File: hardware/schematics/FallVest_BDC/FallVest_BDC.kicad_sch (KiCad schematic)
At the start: 5 parts, among them U1 STP55NF06L, U3 4554

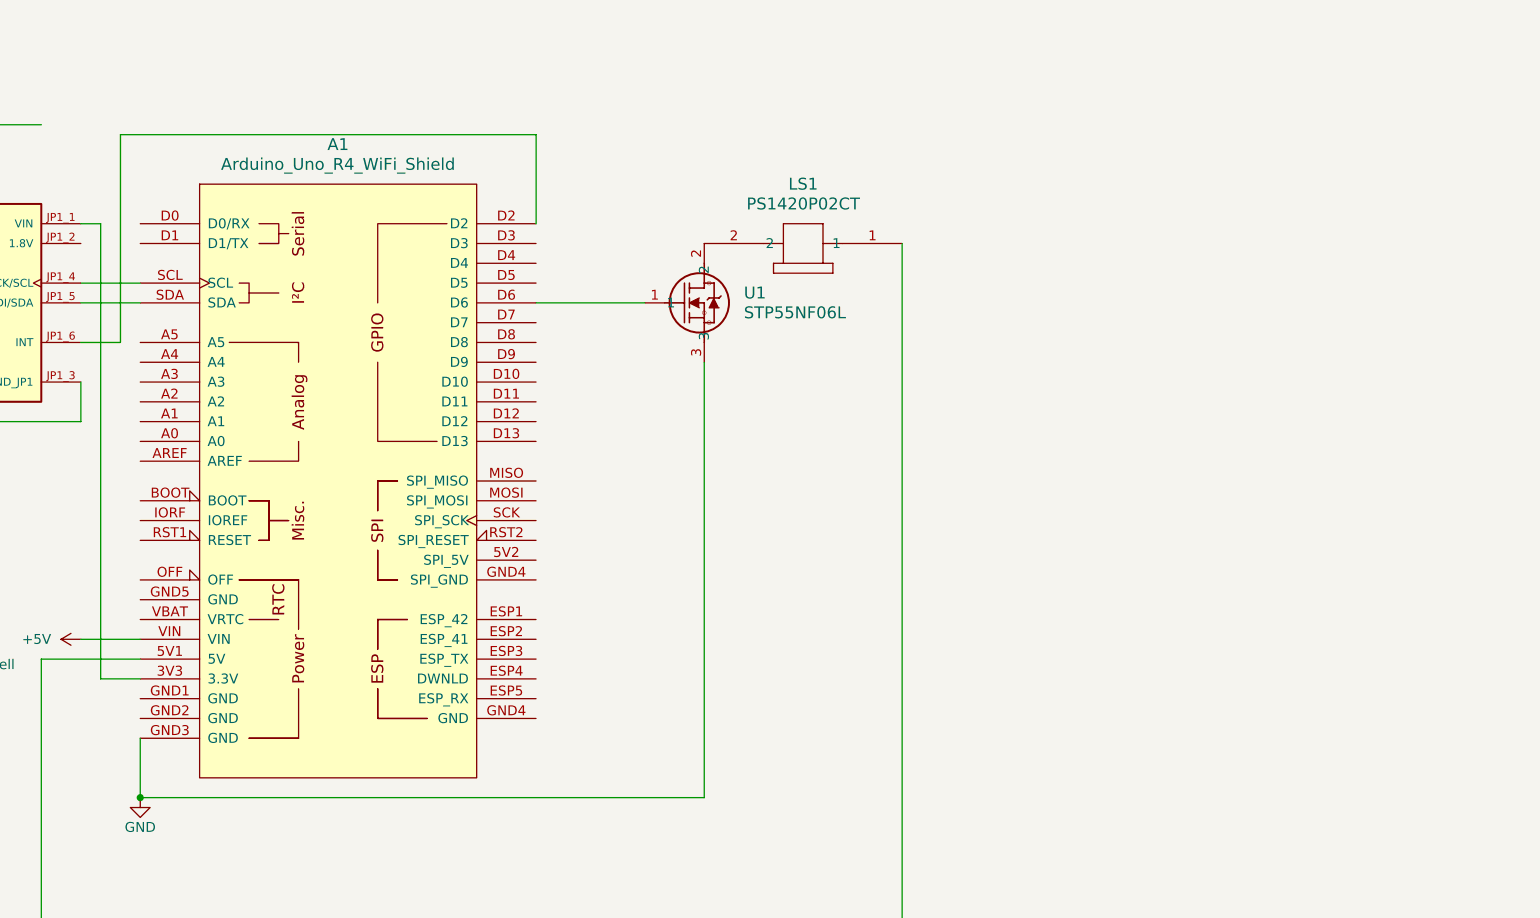
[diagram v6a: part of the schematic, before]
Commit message: Hardware Change
Replaced Uno with ESP 32
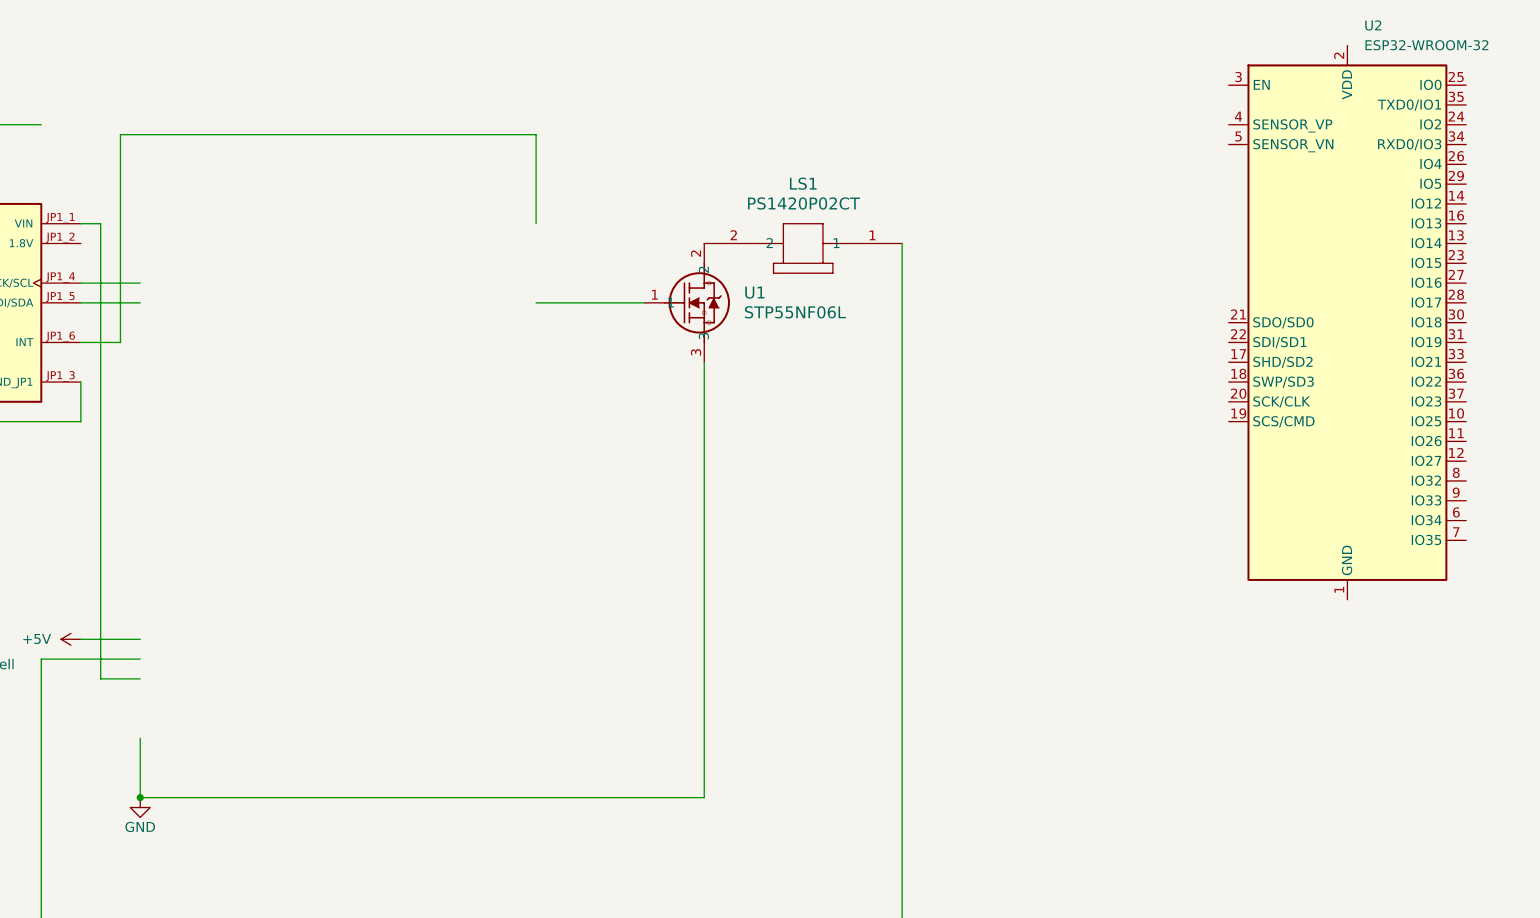
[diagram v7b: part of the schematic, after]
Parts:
- removed A1: Arduino_Uno_R4_WiFi_Shield, PCM_arduino-library:Arduino_Uno_R4_WiFi_Shield, symbol arduino-library:Arduino_Uno_R4_WiFi_Shield
- added U2: ESP32-WROOM-32, RF_Module:ESP32-WROOM-32, symbol RF_Module:ESP32-WROOM-32
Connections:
- new net: U2.1 (GND), U2.15 (GND), U2.38 (GND), U2.39 (GND)
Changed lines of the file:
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@@
+	)
+	(symbol
+		(lib_id "RF_Module:ESP32-WROOM-32")
+		(at 256.54 60.96 0)
+		(unit 1)
+		(exclude_from_sim no)
+		(in_bom yes)
+		(on_board yes)
+		(dnp no)
+		(fields_autoplaced yes)
+		(property "Reference" "U2"
+			(at 258.6833 22.86 0)
+			(effects
+				(font
+					(size 1.27 1.27)
+				)
+				(justify left)
+			)
+		)
+		(property "Value" "ESP32-WROOM-32"
+			(at 258.6833 25.4 0)
+			(effects
+				(font
+					(size 1.27 1.27)
+				)
+				(justify left)
+			)
+		)
+		(property "Footprint" "RF_Module:ESP32-WROOM-32"
+			(at 256.54 99.06 0)
+			(effects
+				(font
+					(size 1.27 1.27)
+				)
+				(hide yes)
+			)
+		)
+		(property "Datasheet" "https://www.espressif.com/sites/default/files/documentation/esp32-wroom-32_datasheet_en.pdf"
+			(at 248.92 59.69 0)
+			(effects
+				(font
+					(size 1.27 1.27)
+				)
+				(hide yes)
+			)
+		)
+		(property "Description" "RF Module, ESP32-D0WDQ6 SoC, Wi-Fi 802.11b/g/n, Bluetooth, BLE, 32-bit, 2.7-3.6V, onboard antenna, SMD"
+			(at 256.54 60.96 0)
+			(effects
+				(font
+					(size 1.27 1.27)
+				)
+				(hide yes)
+			)
+		)
+		(pin "3"
+		)
+		(pin "21"
+		)
+		(pin "15"
+		)
+		(pin "17"
+		)
+		(pin "16"
+		)
+		(pin "31"
+		)
+		(pin "1"
+		)
+		(pin "38"
+		)
+		(pin "22"
+		)
+		(pin "28"
+		)
+		(pin "20"
+		)
+		(pin "32"
+		)
+		(pin "2"
+		)
+		(pin "18"
+		)
+		(pin "39"
+		)
+		(pin "13"
+		)
+		(pin "30"
+		)
+		(pin "27"
+		)
+		(pin "37"
+		)
+		(pin "35"
+		)
+		(pin "34"
+		)
+		(pin "14"
+		)
+		(pin "24"
+		)
+		(pin "29"
+		)
+		(pin "4"
+		)
+		(pin "5"
+		)
+		(pin "19"
+		)
+		(pin "25"
+		)
+		(pin "26"
+		)
+		(pin "23"
+		)
+		(pin "36"
+		)
+		(pin "33"
+		)
+		(pin "10"
+		)
+		(pin "11"
+		)
+		(pin "8"
+		)
+		(pin "7"
+		)
+		(pin "6"
+		)
+		(pin "9"
+		)
+		(pin "12"
+		)
+		(instances
+			(project ""
+				(path "/74063a4b-f2d6-40f5-8694-30dc3de3f53f"
+					(reference "U2")
+					(unit 1)
+				)
+			)
+		)
 	)
 	(symbol
@@
 					(unit 1)
 				)
-			)
-		)
-	)
-	(symbol
-		(lib_id "arduino-library:Arduino_Uno_R4_WiFi_Shield")
-		(at 127 81.28 0)
-		(unit 1)
-		(exclude_from_sim no)
-		(in_bom yes)
-		(on_board yes)
-		(dnp no)
-		(fields_autoplaced yes)
-		(property "Reference" "A1"
-			(at 127 38.1 0)
-			(effects
-				(font
-					(size 1.524 1.524)
-				)
-			)
-		)
-		(property "Value" "Arduino_Uno_R4_WiFi_Shield"
-			(at 127 40.64 0)
-			(effects
-				(font
-					(size 1.524 1.524)
-				)
-			)
-		)
-		(property "Footprint" "PCM_arduino-library:Arduino_Uno_R4_WiFi_Shield"
-			(at 127 127 0)
-			(effects
-				(font
-					(size 1.524 1.524)
-				)
-				(hide yes)
-			)
-		)
-		(property "Datasheet" "https://docs.arduino.cc/hardware/uno-r4-wifi"
-			(at 127 123.19 0)
-			(effects
-				(font
-					(size 1.524 1.524)
-				)
-				(hide yes)
-			)
-		)
-		(property "Description" "Shield for Arduino Uno R4 WiFi"
-			(at 127 81.28 0)
-			(effects
-				(font
-					(size 1.27 1.27)
-				)
-				(hide yes)
-			)
-		)
-		(pin "D1"
-		)
-		(pin "5V1"
-		)
-		(pin "GND2"
-		)
-		(pin "IORF"
-		)
-		(pin "D3"
-		)
-		(pin "D5"
-		)
-		(pin "VBAT"
-		)
-		(pin "A1"
-		)
-		(pin "D0"
-		)
-		(pin "A2"
-		)
-		(pin "A4"
-		)
-		(pin "BOOT"
-		)
-		(pin "A3"
-		)
-		(pin "GND5"
-		)
-		(pin "VIN"
-		)
-		(pin "AREF"
-		)
-		(pin "SDA"
-		)
-		(pin "RST1"
-		)
-		(pin "GND1"
-		)
-		(pin "A0"
-		)
-		(pin "A5"
-		)
-		(pin "SCL"
-		)
-		(pin "OFF"
-		)
-		(pin "3V3"
-		)
-		(pin "GND3"
-		)
-		(pin "D2"
-		)
-		(pin "D4"
-		)
-		(pin "D8"
-		)
-		(pin "MISO"
-		)
-		(pin "GND4"
-		)
-		(pin "ESP4"
-		)
-		(pin "D12"
-		)
-		(pin "ESP5"
-		)
-		(pin "D6"
-		)
-		(pin "RST2"
-		)
-		(pin "D10"
-		)
-		(pin "D11"
-		)
-		(pin "D9"
-		)
-		(pin "ESP1"
-		)
-		(pin "MOSI"
-		)
-		(pin "D13"
-		)
-		(pin "ESP2"
-		)
-		(pin "SCK"
-		)
-		(pin "5V2"
-		)
-		(pin "ESP3"
-		)
-		(pin "GND4"
-		)
-		(pin "D7"
-		)
-		(instances
-			(project ""
-				(path "/74063a4b-f2d6-40f5-8694-30dc3de3f53f"
-					(reference "A1")
-					(unit 1)
-				)

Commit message: NEO6M
I believe I added it for real this time.

Will add SIM800L later and fix wiring.
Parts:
- removed U1: STP55NF06L, TO-220_STM, symbol EE_VEST_SYM:STP55NF06L
- added Q1: AO3400A, Package_TO_SOT_SMD:SOT-23, symbol Transistor_FET:AO3400A
- added U4: NEO-6M, C2927633:GPSM-SMD_24P-L16.0-W12.2-P1.10, symbol NEO-6M:NEO-6M
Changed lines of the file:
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@@
 	(wire
 		(pts
-			(xy 152.4 58.42) (xy 166.37 58.42)
-		)
-		(stroke
-			(width 0)
-			(type default)
-		)
-	)
-	(wire
-		(pts
 			(xy 54.61 35.56) (xy 88.9 35.56)
 		)
@@
 	)
 	(symbol
+		(lib_id "Transistor_FET:AO3400A")
+		(at 40.64 135.89 0)
+		(unit 1)
+		(exclude_from_sim no)
+		(in_bom yes)
+		(on_board yes)
+		(dnp no)
+		(fields_autoplaced yes)
+		(property "Reference" "Q1"
+			(at 46.99 134.6199 0)
+			(effects
+				(font
+					(size 1.27 1.27)
+				)
+				(justify left)
+			)
+		)
+		(property "Value" "AO3400A"
+			(at 46.99 137.1599 0)
+			(effects
+				(font
+					(size 1.27 1.27)
+				)
+				(justify left)
+			)
+		)
+		(property "Footprint" "Package_TO_SOT_SMD:SOT-23"
+			(at 45.72 137.795 0)
+			(effects
+				(font
+					(size 1.27 1.27)
+					(italic yes)
+				)
+				(justify left)
+				(hide yes)
+			)
+		)
+		(property "Datasheet" "http://www.aosmd.com/pdfs/datasheet/AO3400A.pdf"
+			(at 45.72 139.7 0)
+			(effects
+				(font
+					(size 1.27 1.27)
+				)
+				(justify left)
+				(hide yes)
+			)
+		)
+		(property "Description" "30V Vds, 5.7A Id, N-Channel MOSFET, SOT-23"
+			(at 40.64 135.89 0)
+			(effects
+				(font
+					(size 1.27 1.27)
+				)
+				(hide yes)
+			)
+		)
+		(pin "3"
+		)
+		(pin "2"
+		)
+		(pin "1"
+		)
+		(instances
+			(project ""
+				(path "/74063a4b-f2d6-40f5-8694-30dc3de3f53f"
+					(reference "Q1")
+					(unit 1)
+				)
+			)
+		)
+	)
+	(symbol
+		(lib_id "NEO-6M:NEO-6M")
+		(at 40.64 173.99 0)
+		(unit 1)
+		(exclude_from_sim no)
+		(in_bom yes)
+		(on_board yes)
+		(dnp no)
+		(fields_autoplaced yes)
+		(property "Reference" "U4"
+			(at 40.64 152.4 0)
+			(effects
+				(font
+					(size 1.27 1.27)
+				)
+			)
+		)
+		(property "Value" "NEO-6M"
+			(at 40.64 154.94 0)
+			(effects
+				(font
+					(size 1.27 1.27)
+				)
+			)
+		)
+		(property "Footprint" "C2927633:GPSM-SMD_24P-L16.0-W12.2-P1.10"
+			(at 40.64 195.58 0)
+			(effects
+				(font
+					(size 1.27 1.27)
+				)
+				(hide yes)
+			)
+		)
+		(property "Datasheet" "https://www.lcsc.com/datasheet/C2927633.pdf"
+			(at 40.64 198.12 0)
+			(effects
+				(font
+					(size 1.27 1.27)
+				)
+				(hide yes)
+			)
+		)
+		(property "Description" ""
+			(at 40.64 173.99 0)
+			(effects
+				(font
+					(size 1.27 1.27)
+				)
+				(hide yes)
+			)
+		)
+		(property "MPN" "NEO-6M"
+			(at 40.64 200.66 0)
+			(effects
+				(font
+					(size 1.27 1.27)
+				)
+				(hide yes)
+			)
+		)
+		(property "LCSC Part" "C2927633"
+			(at 40.64 203.2 0)
+			(effects
+				(font
+					(size 1.27 1.27)
+				)
+				(hide yes)
+			)
+		)
+		(pin "9"
+		)
+		(pin "10"
+		)
+		(pin "12"
+		)
+		(pin "1"
+		)
+		(pin "7"
+		)
+		(pin "2"
+		)
+		(pin "24"
+		)
+		(pin "5"
+		)
+		(pin "23"
+		)
+		(pin "3"
+		)
+		(pin "22"
+		)
+		(pin "4"
+		)
+		(pin "6"
+		)
+		(pin "8"
+		)
+		(pin "11"
+		)
+		(pin "16"
+		)
+		(pin "17"
+		)
+		(pin "14"
+		)
+		(pin "15"
+		)
+		(pin "18"
+		)
+		(pin "21"
+		)
+		(pin "19"
+		)
+		(pin "20"
+		)
+		(pin "13"
+		)
+		(instances
+			(project ""
+				(path "/74063a4b-f2d6-40f5-8694-30dc3de3f53f"
+					(reference "U4")
+					(unit 1)
+				)
+			)
+		)
+	)
+	(symbol
 		(lib_id "EE_VEST_SYM:4554")
 		(at 41.91 59.69 0)
@@
 					(unit 1)
 				)
-			)
-		)
-	)
-	(symbol
-		(lib_id "EE_VEST_SYM:STP55NF06L")
-		(at 166.37 58.42 0)
-		(unit 1)
-		(exclude_from_sim no)
-		(in_bom yes)
-		(on_board yes)
-		(dnp no)
-		(fields_autoplaced yes)
-		(property "Reference" "U1"
-			(at 179.07 57.1499 0)
-			(effects
-				(font
-					(size 1.524 1.524)
-				)
-				(justify left)
-			)
-		)
-		(property "Value" "STP55NF06L"
-			(at 179.07 59.6899 0)
-			(effects
-				(font
-					(size 1.524 1.524)
-				)
-				(justify left)
-			)
-		)
-		(property "Footprint" "TO-220_STM"
-			(at 166.37 58.42 0)
-			(effects
-				(font
-					(size 1.27 1.27)
-					(italic yes)
-				)
-				(hide yes)
-			)
-		)
-		(property "Datasheet" "https://www.st.com/resource/en/datasheet/stp55nf06l.pdf"
-			(at 166.37 58.42 0)
-			(effects
-				(font
-					(size 1.27 1.27)
-					(italic yes)
-				)
-				(hide yes)
-			)
-		)
-		(property "Description" "https://www.digikey.com/en/products/detail/stmicroelectronics/STP55NF06L/1039551"
-			(at 166.37 58.42 0)
-			(effects
-				(font
-					(size 1.27 1.27)
-				)
-				(hide yes)
-			)
-		)
-		(pin "1"
-		)
-		(pin "2"
-		)
-		(pin "3"
-		)
-		(instances
-			(project ""
-				(path "/74063a4b-f2d6-40f5-8694-30dc3de3f53f"
-					(reference "U1")
-					(unit 1)
-				)
